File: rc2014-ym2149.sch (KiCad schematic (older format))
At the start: 28 parts, among them J1 AUDIO OUT, J2 IO Out, P1 RC2014 BUS, U1 74HCT138, U2 74HCT138, U3 74HCT00, U4 74HCT74, U5 AY-3-8190/YM2149F

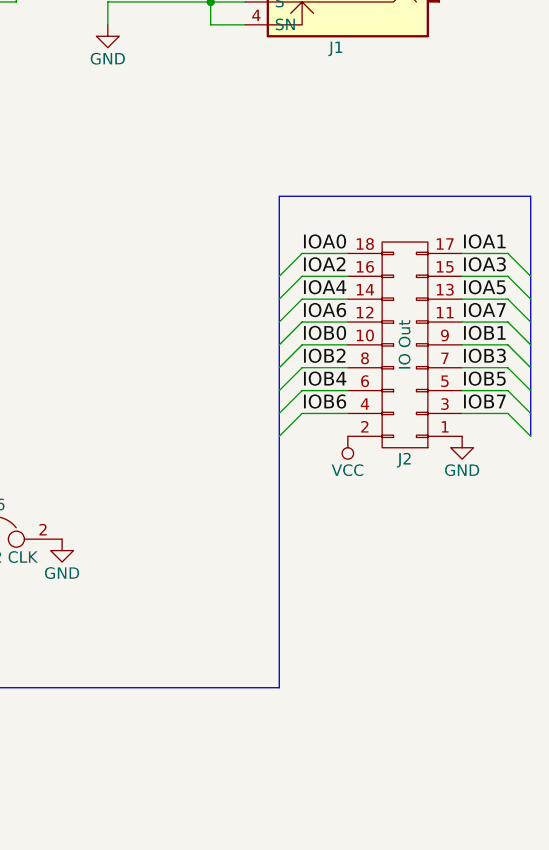
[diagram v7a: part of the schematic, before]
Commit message: More test programs and changes for Rev 3 PCB
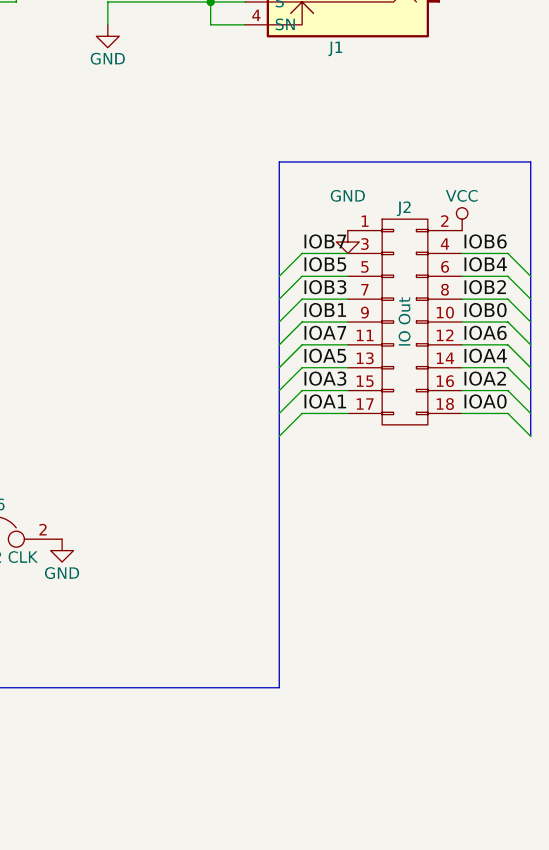
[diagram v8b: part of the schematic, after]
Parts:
- R1, R2, R3, R4, R5, R6, R7: footprint Resistors_THT:R_Axial_DIN0207_L6.3mm_D2.5mm_P7.62mm_Horizontal -> rc2014:R_Axial_DIN0207_L6.3mm_D2.5mm_P10.16mm_Horizontal
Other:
- moved on the sheet: J2
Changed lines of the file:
@@
 L CONN_02X09 J2
 U 1 1 58BC7A79
-P 10450 2700
-F 0 "J2" H 10450 3200 50  0000 C CNN
-F 1 "IO Out" V 10450 2700 50  0000 C CNN
-F 2 "Pin_Headers:Pin_Header_Straight_2x09_Pitch2.54mm" H 10450 1500 50  0001 C CNN
-F 3 "" H 10450 1500 50  0000 C CNN
-	1    10450 2700
-	-1   0    0    1
-$EndComp
-Text Label 10000 2300 0    60   ~ 0
+P 10450 2600
+F 0 "J2" H 10450 3100 50  0000 C CNN
+F 1 "IO Out" V 10450 2600 50  0000 C CNN
+F 2 "Pin_Headers:Pin_Header_Straight_2x09_Pitch2.54mm" H 10450 1400 50  0001 C CNN
+F 3 "" H 10450 1400 50  0000 C CNN
+	1    10450 2600
+	1    0    0    -1
+$EndComp
+Text Label 10900 3000 2    60   ~ 0
 IOA0
-Text Label 10700 2300 0    60   ~ 0
+Text Label 10200 3000 2    60   ~ 0
 IOA1
-Text Label 10000 2400 0    60   ~ 0
+Text Label 10900 2900 2    60   ~ 0
 IOA2
-Text Label 10700 2400 0    60   ~ 0
+Text Label 10200 2900 2    60   ~ 0
 IOA3
-Text Label 10000 2500 0    60   ~ 0
+Text Label 10900 2800 2    60   ~ 0
 IOA4
-Text Label 10700 2500 0    60   ~ 0
+Text Label 10200 2800 2    60   ~ 0
 IOA5
-Text Label 10000 2600 0    60   ~ 0
+Text Label 10900 2700 2    60   ~ 0
 IOA6
-Text Label 10700 2600 0    60   ~ 0
+Text Label 10200 2700 2    60   ~ 0
 IOA7
-Text Label 10000 2700 0    60   ~ 0
+Text Label 10900 2600 2    60   ~ 0
 IOB0
-Text Label 10700 2700 0    60   ~ 0
+Text Label 10200 2600 2    60   ~ 0
 IOB1
-Text Label 10000 2800 0    60   ~ 0
+Text Label 10900 2500 2    60   ~ 0
 IOB2
-Text Label 10700 2800 0    60   ~ 0
+Text Label 10200 2500 2    60   ~ 0
 IOB3
-Text Label 10000 2900 0    60   ~ 0
+Text Label 10900 2400 2    60   ~ 0
 IOB4
-Text Label 10700 2900 0    60   ~ 0
+Text Label 10200 2400 2    60   ~ 0
 IOB5
-Text Label 10000 3000 0    60   ~ 0
+Text Label 10900 2300 2    60   ~ 0
 IOB6
-Text Label 10700 3000 0    60   ~ 0
+Text Label 10200 2300 2    60   ~ 0
 IOB7
 $Comp
 L VCC #PWR014
 U 1 1 58BC8268
-P 10200 3100
-F 0 "#PWR014" H 10200 2950 50  0001 C CNN
-F 1 "VCC" H 10200 3250 50  0000 C CNN
-F 2 "" H 10200 3100 50  0000 C CNN
-F 3 "" H 10200 3100 50  0000 C CNN
-	1    10200 3100
-	-1   0    0    1
+P 10700 2200
+F 0 "#PWR014" H 10700 2050 50  0001 C CNN
+F 1 "VCC" H 10700 2350 50  0000 C CNN
+F 2 "" H 10700 2200 50  0000 C CNN
+F 3 "" H 10700 2200 50  0000 C CNN
+	1    10700 2200
+	1    0    0    -1
 $EndComp
 $Comp
 L GND #PWR015
 U 1 1 58BC829C
-P 10700 3100
-F 0 "#PWR015" H 10700 2850 50  0001 C CNN
-F 1 "GND" H 10700 2950 50  0000 C CNN
-F 2 "" H 10700 3100 50  0000 C CNN
-F 3 "" H 10700 3100 50  0000 C CNN
-	1    10700 3100
+P 10200 2200
+F 0 "#PWR015" H 10200 1950 50  0001 C CNN
+F 1 "GND" H 10200 2350 50  0000 C CNN
+F 2 "" H 10200 2200 50  0000 C CNN
+F 3 "" H 10200 2200 50  0000 C CNN
+	1    10200 2200
 	1    0    0    -1
 $EndComp
@@
 F 0 "R4" H 8330 620 50  0000 L CNN
 F 1 "1K" H 8330 560 50  0000 L CNN
-F 2 "Resistors_THT:R_Axial_DIN0207_L6.3mm_D2.5mm_P7.62mm_Horizontal" H 8300 600 50  0001 C CNN
+F 2 "rc2014:R_Axial_DIN0207_L6.3mm_D2.5mm_P10.16mm_Horizontal" H 8300 600 50  0001 C CNN
 F 3 "" H 8300 600 50  0000 C CNN
 F 4 "MF25 1K" H 8300 600 60  0001 C CNN "MPN"
@@
 F 0 "R5" H 8330 820 50  0000 L CNN
 F 1 "1K" H 8330 760 50  0000 L CNN
-F 2 "Resistors_THT:R_Axial_DIN0207_L6.3mm_D2.5mm_P7.62mm_Horizontal" H 8300 800 50  0001 C CNN
+F 2 "rc2014:R_Axial_DIN0207_L6.3mm_D2.5mm_P10.16mm_Horizontal" H 8300 800 50  0001 C CNN
 F 3 "" H 8300 800 50  0000 C CNN
 	1    8300 800
@@
 F 0 "R6" H 8330 1020 50  0000 L CNN
 F 1 "1K6" H 8330 960 50  0000 L CNN
-F 2 "Resistors_THT:R_Axial_DIN0207_L6.3mm_D2.5mm_P7.62mm_Horizontal" H 8300 1000 50  0001 C CNN
+F 2 "rc2014:R_Axial_DIN0207_L6.3mm_D2.5mm_P10.16mm_Horizontal" H 8300 1000 50  0001 C CNN
 F 3 "" H 8300 1000 50  0000 C CNN
 F 4 "MF25 1K6" H 8300 1000 60  0001 C CNN "MPN"
@@
 F 0 "R7" H 8330 1220 50  0000 L CNN
 F 1 "1K6" H 8330 1160 50  0000 L CNN
-F 2 "Resistors_THT:R_Axial_DIN0207_L6.3mm_D2.5mm_P7.62mm_Horizontal" H 8300 1200 50  0001 C CNN
+F 2 "rc2014:R_Axial_DIN0207_L6.3mm_D2.5mm_P10.16mm_Horizontal" H 8300 1200 50  0001 C CNN
 F 3 "" H 8300 1200 50  0000 C CNN
 	1    8300 1200
@@
 F 0 "R2" H 7630 1370 50  0000 L CNN
 F 1 "470R" H 7630 1310 50  0000 L CNN
-F 2 "Resistors_THT:R_Axial_DIN0207_L6.3mm_D2.5mm_P7.62mm_Horizontal" H 7600 1350 50  0001 C CNN
+F 2 "rc2014:R_Axial_DIN0207_L6.3mm_D2.5mm_P10.16mm_Horizontal" H 7600 1350 50  0001 C CNN
 F 3 "" H 7600 1350 50  0000 C CNN
 	1    7600 1350
@@
 F 0 "R1" H 7330 1370 50  0000 L CNN
 F 1 "470R" H 7330 1310 50  0000 L CNN
-F 2 "Resistors_THT:R_Axial_DIN0207_L6.3mm_D2.5mm_P7.62mm_Horizontal" H 7300 1350 50  0001 C CNN
+F 2 "rc2014:R_Axial_DIN0207_L6.3mm_D2.5mm_P10.16mm_Horizontal" H 7300 1350 50  0001 C CNN
 F 3 "" H 7300 1350 50  0000 C CNN
 F 4 "MF25 470R" H 7300 1350 60  0001 C CNN "MPN"
@@
 F 0 "R3" H 7930 1370 50  0000 L CNN
 F 1 "470R" H 7930 1310 50  0000 L CNN
-F 2 "Resistors_THT:R_Axial_DIN0207_L6.3mm_D2.5mm_P7.62mm_Horizontal" H 7900 1350 50  0001 C CNN
+F 2 "rc2014:R_Axial_DIN0207_L6.3mm_D2.5mm_P10.16mm_Horizontal" H 7900 1350 50  0001 C CNN
 F 3 "" H 7900 1350 50  0000 C CNN
 	1    7900 1350
@@
 	6000 4200 9900 4200
 Wire Wire Line
+	10700 3000 10900 3000
+Wire Wire Line
+	10700 2900 10900 2900
+Wire Wire Line
+	10700 2800 10900 2800
+Wire Wire Line
+	10700 2700 10900 2700
+Wire Wire Line
+	10700 2600 10900 2600
+Wire Wire Line
+	10700 2500 10900 2500
+Wire Wire Line
+	10700 2400 10900 2400
+Wire Wire Line
+	10700 2300 10900 2300
+Wire Wire Line
+	10200 3000 10000 3000
+Wire Wire Line
+	10200 2900 10000 2900
+Wire Wire Line
+	10200 2800 10000 2800
+Wire Wire Line
+	10200 2700 10000 2700
+Wire Wire Line
+	10200 2600 10000 2600
+Wire Wire Line
+	10200 2500 10000 2500
+Wire Wire Line
+	10200 2400 10000 2400
+Wire Wire Line
 	10200 2300 10000 2300
-Wire Wire Line
-	10200 2400 10000 2400
-Wire Wire Line
-	10200 2500 10000 2500
-Wire Wire Line
-	10200 2600 10000 2600
-Wire Wire Line
-	10200 2700 10000 2700
-Wire Wire Line
-	10200 2800 10000 2800
-Wire Wire Line
-	10200 2900 10000 2900
-Wire Wire Line
-	10200 3000 10000 3000
-Wire Wire Line
-	10700 2300 10900 2300
-Wire Wire Line
-	10700 2400 10900 2400
-Wire Wire Line
-	10700 2500 10900 2500
-Wire Wire Line
-	10700 2600 10900 2600
-Wire Wire Line
-	10700 2700 10900 2700
-Wire Wire Line
-	10700 2800 10900 2800
-Wire Wire Line
-	10700 2900 10900 2900
-Wire Wire Line
-	10700 3000 10900 3000
-Wire Bus Line
-	9900 4200 9900 2050
-Wire Bus Line
-	9900 2050 11000 2050
-Wire Bus Line
-	11000 2050 11000 3100
 Wire Wire Line
 	7350 4050 7350 4100
@@
 Wire Wire Line
 	3950 1500 3800 1500
+Wire Bus Line
+	9900 4200 9900 1900
+Wire Bus Line
+	9900 1900 11000 1900
+Wire Bus Line
+	11000 1900 11000 3100
 $EndSCHEMATC
